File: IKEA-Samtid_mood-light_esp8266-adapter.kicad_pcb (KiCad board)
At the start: 2 copper layers, 17.5 x 20.5 mm, 5 parts, among them P1 ESP8266, P2 mood-light, U1 AMS1117-3.3

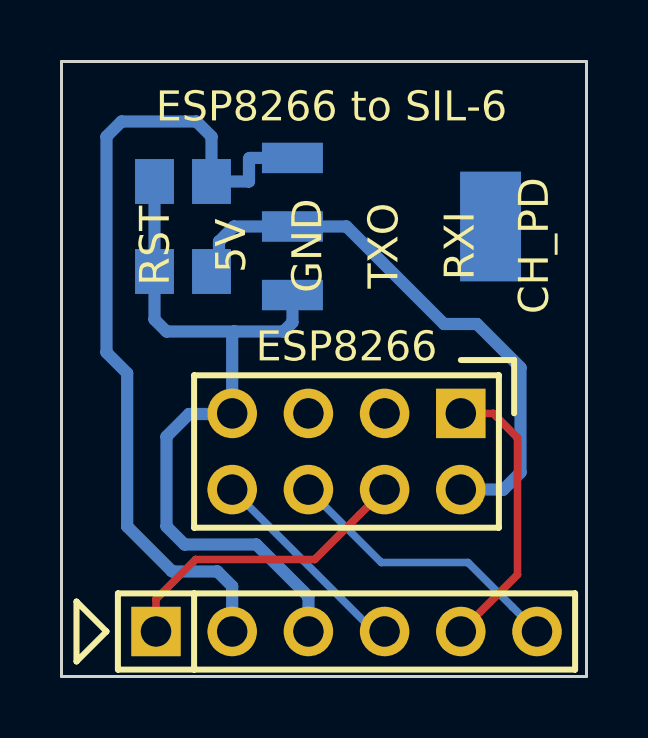
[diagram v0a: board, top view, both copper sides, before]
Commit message: ESP8266 adapter board reduced in size.
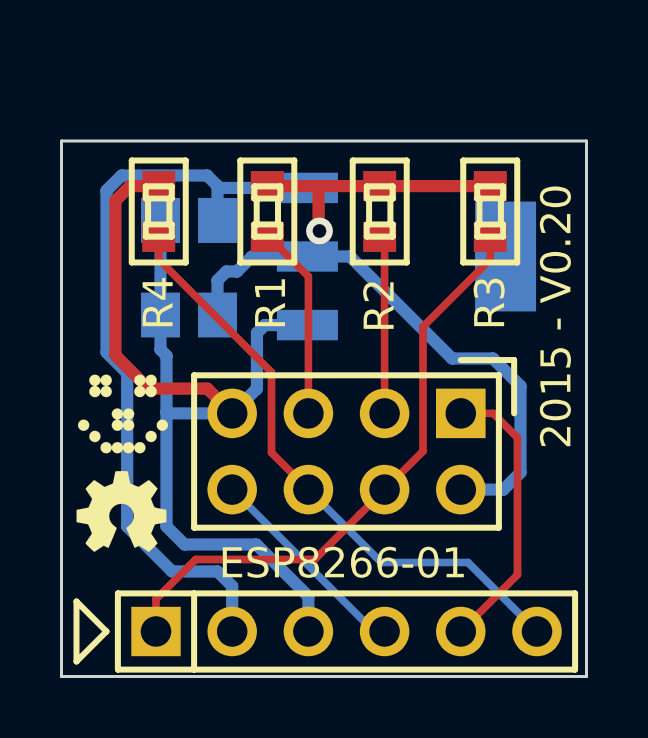
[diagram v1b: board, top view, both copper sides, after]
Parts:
- added G***: LED_smile_silkscreen_3mm, led-smile:LED_smile_silkscreen_3mm, F.Cu at (157.1, 109.8)
- added G***: OSHW-logo_silkscreen_3mm, oshw-logo:OSHW-logo_silkscreen_3mm, F.Cu at (157.0, 113.0)
- added R1: 10k, my_parts:MADW__R0603_2, F.Cu at (161.9, 103.0)
- added R2: 10k, my_parts:MADW__R0603_2, F.Cu at (165.6, 103.0)
- added R3: 10k, my_parts:MADW__R0603_2, F.Cu at (169.3, 103.0)
- added R4: 10k, my_parts:MADW__R0603_2, F.Cu at (158.2, 103.0)
- P1: value ESP8266 -> ESP8266-01
- moved C2 1.46 mm to (159.3, 106.5)
- moved C1 1.32 mm to (159.2, 103.3)
- moved U1 1.12 mm to (166.5, 104.5)
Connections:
- P1 pad 1: /RXI -> /TXO
- P1 pad 3: (no net) -> Net-(P1-Pad3)
- P1 pad 5: (no net) -> Net-(P1-Pad5)
- P1 pad 8: /TXO -> /RXI
- P2 pad 4: /TXO -> /RXI
- P2 pad 5: /RXI -> /TXO
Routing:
- net /CH_PD: track 9.58 -> 20.1 mm
- net GND: track 25.5 -> 35.7 mm
- net /RST: track 10.2 -> 20.1 mm
- net +3.3V: track 19.0 -> 28.4 mm, vias 0 -> 1
- net Net-(P1-Pad5): track 0.00 -> 6.48 mm
- net Net-(P1-Pad3): track 0.00 -> 5.95 mm
- net +5V: track 28.4 -> 25.5 mm
- net /TXO: track 7.39 -> 9.47 mm
- net /RXI: track 9.47 -> 7.39 mm
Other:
- board size 17.5 x 20.5 mm -> 17.5 x 17.8 mm
- net class Power: via_drill 0.635 -> 0.4572
- board text added: "-"
- board text added: "/CH_PD"
- board text added: "/RST"
- board text added: "2015 - V0.20"
- board text added: "3.3V SIG. !"
- board text added: "RX"
- board text added: "TX"
- board text removed: "CH_PD"
- board text removed: "ESP8266 to SIL-6"
- board text removed: "GND"
- board text removed: "RST"
- board text removed: "RXI"
- board text removed: "TXO"

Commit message: ESP8266 adapter tweaks.
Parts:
- U1: value AMS1117-3.3 -> AMS1117
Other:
- board text added: "2015 - V0.20.b"
- board text added: "AMS1117"
- board text removed: "2015 - V0.20"

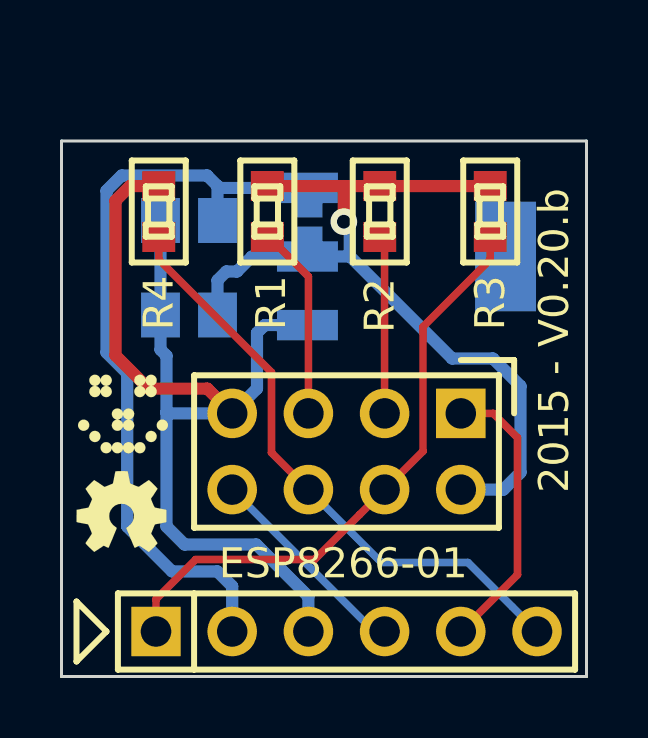
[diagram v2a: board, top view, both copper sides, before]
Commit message: Added pads for ESP8266 FW upd. mode (GPIO0 shorted to GND) on startup.
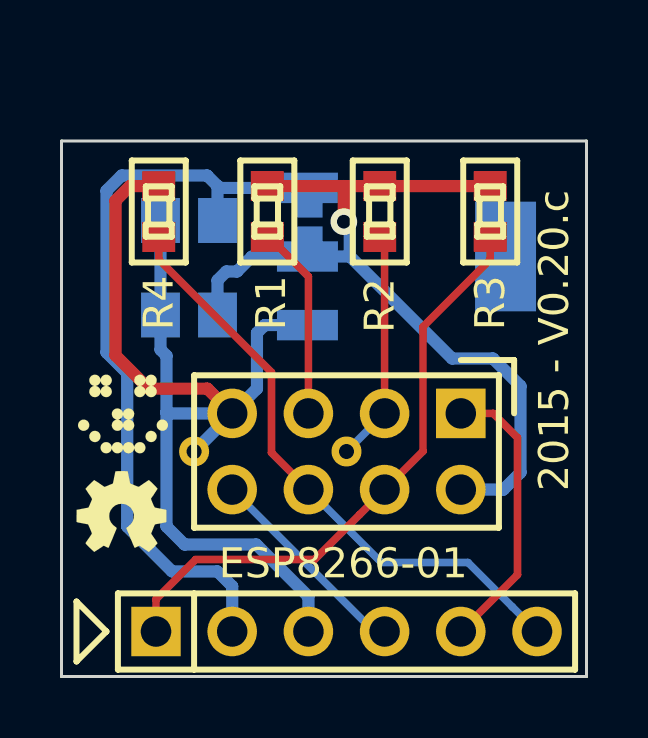
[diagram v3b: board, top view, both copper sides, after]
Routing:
- net Net-(P1-Pad3): track 5.95 -> 7.74 mm
- net GND: track 35.7 -> 37.5 mm
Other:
- board text added: "2015 - V0.20.c"
- board text added: "3.3V SIG"
- board text added: "FW UP"
- board text removed: "2015 - V0.20.b"
- board text removed: "3.3V SIG. !"
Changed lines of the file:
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@@
 (kicad_pcb (version 4) (host pcbnew "(2015-03-12 BZR 5508)-product")
   (general
-    (links 27)
-    (no_connects 3)
+    (links 24)
+    (no_connects 0)
     (area 154.481657 100.599999 181.95 123.450001)
     (thickness 1.6)
-    (drawings 15)
-    (tracks 95)
+    (drawings 16)
+    (tracks 97)
     (zones 0)
     (modules 11)
@@
     (title IKEA-Samtid_mood-light_esp8266-adapter)
     (date "Thu 12 Mar 2015")
-    (rev 0.20.b)
+    (rev 0.20.c)
     (company "2015 - blog.spitzenpfeil.org")
   )
@@
     (add_net GND)
   )
+  (module DIL-Headers:DIL-4 (layer F.Cu)
+    (at 164.5 111)
+    (descr "Male 3x2 header with 2.54mm raster")
+    (tags "CONN, header, male, 3x2, 2.54mm")
+    (fp_text reference P1 (at 0 -3.81) (layer F.SilkS) hide
+      (effects (font (size 1 1) (thickness 0.2)))
+    )
+    (fp_text value ESP8266-01 (at -0.11 3.73) (layer F.SilkS)
+      (effects (font (size 1 1) (thickness 0.2)))
+    )
+    (fp_line (start -4.191 0) (end -0.889 0) (layer B.SilkS) (width 0.2))
+    (fp_circle (center -5.08 0) (end -4.318 0) (layer B.SilkS) (width 0.2))
+    (fp_circle (center 0 0) (end 0.762 0) (layer B.SilkS) (width 0.2))
+    (fp_line (start 5.588 -3.048) (end 5.588 -1.27) (layer F.SilkS) (width 0.2))
+    (fp_line (start 3.81 -3.048) (end 5.588 -3.048) (layer F.SilkS) (width 0.2))
+    (fp_line (start 5.08 -2.54) (end 5.08 2.54) (layer F.SilkS) (width 0.2))
+    (fp_line (start -5.08 -2.54) (end 5.08 -2.54) (layer F.SilkS) (width 0.2))
+    (fp_line (start 5.08 2.54) (end -5.08 2.54) (layer F.SilkS) (width 0.2))
+    (fp_line (start -5.08 2.54) (end -5.08 -2.54) (layer F.SilkS) (width 0.2))
+    (pad 1 thru_hole rect (at 3.81 -1.27) (size 1.651 1.651) (drill 1.016) (layers *.Cu *.Mask F.SilkS)
+      (net 7 /TXO))
+    (pad 2 thru_hole circle (at 3.81 1.27) (size 1.651 1.651) (drill 1.016) (layers *.Cu *.Mask F.SilkS)
+      (net 3 +3.3V))
+    (pad 3 thru_hole circle (at 1.27 -1.27) (size 1.651 1.651) (drill 1.016) (layers *.Cu *.Mask F.SilkS)
+      (net 8 "Net-(P1-Pad3)"))
+    (pad 4 thru_hole circle (at 1.27 1.27) (size 1.651 1.651) (drill 1.016) (layers *.Cu *.Mask F.SilkS)
+      (net 5 /RST))
+    (pad 5 thru_hole circle (at -1.27 -1.27) (size 1.651 1.651) (drill 1.016) (layers *.Cu *.Mask F.SilkS)
+      (net 9 "Net-(P1-Pad5)"))
+    (pad 6 thru_hole circle (at -1.27 1.27) (size 1.651 1.651) (drill 1.016) (layers *.Cu *.Mask F.SilkS)
+      (net 6 /CH_PD))
+    (pad 7 thru_hole circle (at -3.81 -1.27) (size 1.651 1.651) (drill 1.016) (layers *.Cu *.Mask F.SilkS)
+      (net 2 GND))
+    (pad 8 thru_hole circle (at -3.81 1.27) (size 1.651 1.651) (drill 1.016) (layers *.Cu *.Mask F.SilkS)
+      (net 4 /RXI))
+    (pad 3 thru_hole circle (at 0 0) (size 1 1) (drill 0.5) (layers *.Cu *.Mask F.SilkS)
+      (net 8 "Net-(P1-Pad3)"))
+    (pad 7 thru_hole circle (at -5.08 0) (size 1 1) (drill 0.5) (layers *.Cu *.Mask F.SilkS)
+      (net 2 GND))
+  )
   (module SMD_Packages:SOT-223 (layer B.Cu)
     (at 166.5 104.5 90)
@@
     (pad 6 thru_hole circle (at 6.35 0) (size 1.65 1.65) (drill 1.016) (layers *.Cu *.Mask F.SilkS)
       (net 6 /CH_PD))
-  )
-  (module DIL-Headers:DIL-4 (layer F.Cu)
-    (at 164.5 111)
-    (descr "Male 3x2 header with 2.54mm raster")
-    (tags "CONN, header, male, 3x2, 2.54mm")
-    (fp_text reference P1 (at 0 -3.81) (layer F.SilkS) hide
-      (effects (font (size 1 1) (thickness 0.2)))
-    )
-    (fp_text value ESP8266-01 (at -0.11 3.73) (layer F.SilkS)
-      (effects (font (size 1 1) (thickness 0.2)))
-    )
-    (fp_line (start 5.588 -3.048) (end 5.588 -1.27) (layer F.SilkS) (width 0.2))
-    (fp_line (start 3.81 -3.048) (end 5.588 -3.048) (layer F.SilkS) (width 0.2))
-    (fp_line (start 5.08 -2.54) (end 5.08 2.54) (layer F.SilkS) (width 0.2))
-    (fp_line (start -5.08 -2.54) (end 5.08 -2.54) (layer F.SilkS) (width 0.2))
-    (fp_line (start 5.08 2.54) (end -5.08 2.54) (layer F.SilkS) (width 0.2))
-    (fp_line (start -5.08 2.54) (end -5.08 -2.54) (layer F.SilkS) (width 0.2))
-    (pad 1 thru_hole rect (at 3.81 -1.27) (size 1.651 1.651) (drill 1.016) (layers *.Cu *.Mask F.SilkS)
-      (net 7 /TXO))
-    (pad 2 thru_hole circle (at 3.81 1.27) (size 1.651 1.651) (drill 1.016) (layers *.Cu *.Mask F.SilkS)
-      (net 3 +3.3V))
-    (pad 3 thru_hole circle (at 1.27 -1.27) (size 1.651 1.651) (drill 1.016) (layers *.Cu *.Mask F.SilkS)
-      (net 8 "Net-(P1-Pad3)"))
-    (pad 4 thru_hole circle (at 1.27 1.27) (size 1.651 1.651) (drill 1.016) (layers *.Cu *.Mask F.SilkS)
-      (net 5 /RST))
-    (pad 5 thru_hole circle (at -1.27 -1.27) (size 1.651 1.651) (drill 1.016) (layers *.Cu *.Mask F.SilkS)
-      (net 9 "Net-(P1-Pad5)"))
-    (pad 6 thru_hole circle (at -1.27 1.27) (size 1.651 1.651) (drill 1.016) (layers *.Cu *.Mask F.SilkS)
-      (net 6 /CH_PD))
-    (pad 7 thru_hole circle (at -3.81 -1.27) (size 1.651 1.651) (drill 1.016) (layers *.Cu *.Mask F.SilkS)
-      (net 2 GND))
-    (pad 8 thru_hole circle (at -3.81 1.27) (size 1.651 1.651) (drill 1.016) (layers *.Cu *.Mask F.SilkS)
-      (net 4 /RXI))
   )
   (module my_parts:MADW__R0603_2 (layer F.Cu)
@@
       (xy -0.90932 1.3462)) (layer F.SilkS) (width 0.00254))
   )
+  (gr_text "FW\nUP" (at 158.04 109.29 90) (layer B.SilkS)
+    (effects (font (size 1 1) (thickness 0.2)) (justify mirror))
+  )
   (gr_text AMS1117 (at 166.4 104.55 90) (layer B.SilkS)
-    (effects (font (size 1 1) (thickness 0.25)) (justify mirror))
-  )
-  (gr_text "2015 - V0.20.b" (at 171.42 107.3 90) (layer F.SilkS)
-    (effects (font (size 1 1) (thickness 0.25)))
+    (effects (font (size 1 1) (thickness 0.2)) (justify mirror))
+  )
+  (gr_text "2015 - V0.20.c" (at 171.42 107.3 90) (layer F.SilkS)
+    (effects (font (size 1 1) (thickness 0.2)))
   )
   (dimension 17.85 (width 0.3) (layer Eco1.User)
@@
     (arrow2b (pts (xy 173.95 118.5) (xy 173.363579 117.373496)))
   )
-  (gr_text "3.3V SIG. !" (at 155.97 114.13 90) (layer B.SilkS)
-    (effects (font (size 1 1) (thickness 0.25)) (justify mirror))
-  )
-  (gr_text /CH_PD (at 170.815 112.776 90) (layer B.SilkS)
-    (effects (font (size 1 1) (thickness 0.25)) (justify mirror))
-  )
-  (gr_text RX (at 168.275 114.554 90) (layer B.SilkS)
-    (effects (font (size 1 1) (thickness 0.25)) (justify mirror))
-  )
-  (gr_text TX (at 165.862 114.554 90) (layer B.SilkS)
-    (effects (font (size 1 1) (thickness 0.25)) (justify mirror))
-  )
-  (gr_text - (at 163.195 114.554 90) (layer B.SilkS)
-    (effects (font (size 1 1) (thickness 0.25)) (justify mirror))
-  )
-  (gr_text 5V (at 160.655 114.427 90) (layer B.SilkS)
-    (effects (font (size 1 1) (thickness 0.25)) (justify mirror))
-  )
-  (gr_text /RST (at 158.17 113.38 90) (layer B.SilkS)
-    (effects (font (size 1 1) (thickness 0.25)) (justify mirror))
+  (gr_text "3.3V SIG" (at 155.94 115.02 90) (layer B.SilkS)
+    (effects (font (size 1 1) (thickness 0.2)) (justify mirror))
+  )
+  (gr_text /CH_PD (at 170.85 112.97 90) (layer B.SilkS)
+    (effects (font (size 1 1) (thickness 0.2)) (justify mirror))
+  )
+  (gr_text RX (at 168.3 114.87 90) (layer B.SilkS)
+    (effects (font (size 1 1) (thickness 0.2)) (justify mirror))
+  )
+  (gr_text TX (at 165.78 114.99 90) (layer B.SilkS)
+    (effects (font (size 1 1) (thickness 0.2)) (justify mirror))
+  )
+  (gr_text - (at 163.15 115.31 90) (layer B.SilkS)
+    (effects (font (size 1 1) (thickness 0.2)) (justify mirror))
+  )
+  (gr_text 5V (at 160.66 114.89 90) (layer B.SilkS)
+    (effects (font (size 1 1) (thickness 0.2)) (justify mirror))
+  )
+  (gr_text /RST (at 158.17 113.92 90) (layer B.SilkS)
+    (effects (font (size 1 1) (thickness 0.2)) (justify mirror))
   )
   (dimension 17.5 (width 0.3) (layer Eco1.User)
@@
   (segment (start 158.30004 106.44996) (end 158.30008 106.45) (width 0.4064) (layer B.Cu) (net 2))
   (segment (start 158.30004 103.3) (end 158.30004 106.44996) (width 0.4064) (layer B.Cu) (net 2))
+  (segment (start 159.42 111) (end 160.69 109.73) (width 0.4064) (layer B.Cu) (net 2))
   (segment (start 164.6204 104.5) (end 164.61 104.4896) (width 0.4064) (layer B.Cu) (net 3))
   (segment (start 164.61 104.4896) (end 164.61 103.538739) (width 0.4064) (layer B.Cu) (net 3))
@@
   (segment (start 165.77 104.01036) (end 165.608 103.84836) (width 0.254) (layer F.Cu) (net 8))
   (segment (start 165.77 109.73) (end 165.77 104.01036) (width 0.254) (layer F.Cu) (net 8))
+  (segment (start 164.5 111) (end 165.77 109.73) (width 0.254) (layer B.Cu) (net 8))
   (segment (start 161.9123 103.84836) (end 161.8615 103.84836) (width 0.254) (layer F.Cu) (net 9))
   (segment (start 163.23 105.16606) (end 161.9123 103.84836) (width 0.254) (layer F.Cu) (net 9))

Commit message: ESP8266 adapter: changed RX/TX netnames to avoid confusion.
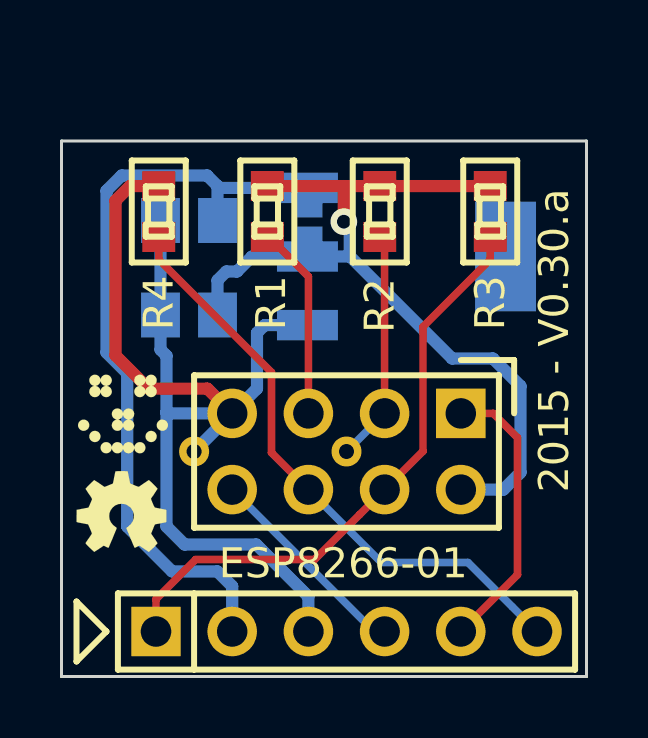
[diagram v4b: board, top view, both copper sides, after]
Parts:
- U1: value AMS1117 -> AMS1117-3.3
- renumbered G*** to G1, G*** to G2
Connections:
- P1 pad 1: /TXO -> /RXI
- P1 pad 8: /RXI -> /TXO
- P2 pad 4: /RXI -> /TXO
- P2 pad 5: /TXO -> /RXI
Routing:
- net /TXO: track 9.47 -> 7.39 mm
- net /RXI: track 7.39 -> 9.47 mm
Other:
- board text added: "2015 - V0.30.a"
- board text removed: "2015 - V0.20.c"

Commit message: ESP8266 adapter: silkscreen tweaks (show pull-up/down status).
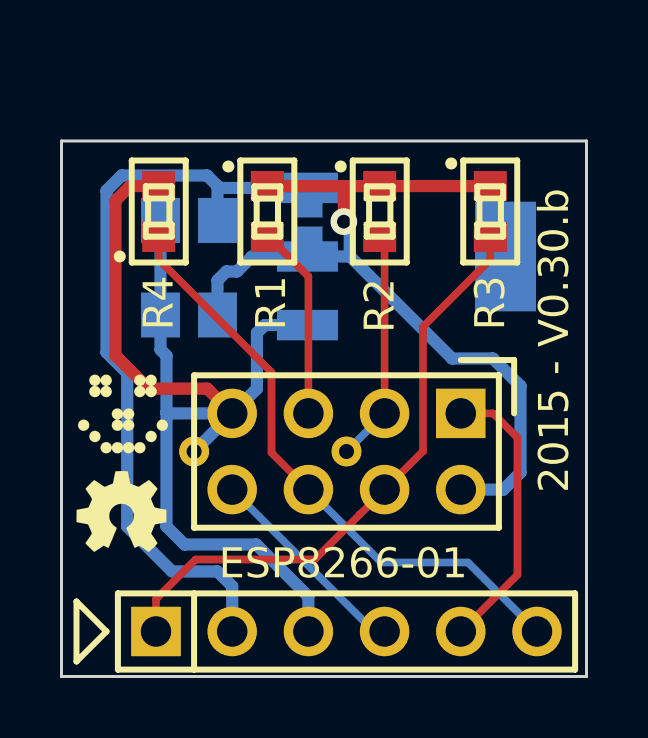
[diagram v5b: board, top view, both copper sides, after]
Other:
- board text added: "2015 - V0.30.b"
- board text added: "~CH_PD~↓"
- board text added: "~RST~↑"
- board text removed: "/CH_PD"
- board text removed: "/RST"
- board text removed: "2015 - V0.30.a"

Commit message: ESP8266 adapter tweaks + added shortened github link on copper.
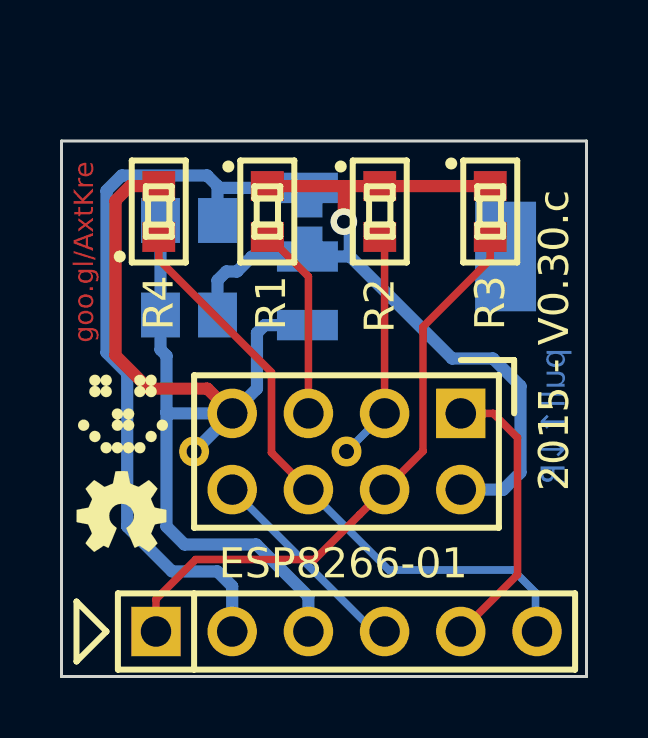
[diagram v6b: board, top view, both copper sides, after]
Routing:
- net /CH_PD: track 20.1 -> 20.8 mm
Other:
- board text added: "2015 - V0.30.c"
- board text added: "AUX 3.3V reg."
- board text added: "EN↓"
- board text added: "goo.gl/AxtKre"
- board text added: "pull↑↓R"
- board text removed: "2015 - V0.30.b"
- board text removed: "~CH_PD~↓"
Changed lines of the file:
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@@
     (area 154.481657 100.599999 181.95 123.450001)
     (thickness 1.6)
-    (drawings 16)
-    (tracks 97)
+    (drawings 19)
+    (tracks 98)
     (zones 0)
     (modules 11)
@@
     (title IKEA-Samtid_mood-light_esp8266-adapter)
     (date "Fri 13 Mar 2015")
-    (rev 0.30.b)
+    (rev 0.30.c)
     (company "2015 - blog.spitzenpfeil.org")
   )
@@
     (mod_text_width 0.15)
     (pad_size 1 1)
-    (pad_drill 0)
+    (pad_drill 0.5)
     (pad_to_mask_clearance 0.0254)
     (aux_axis_origin 0 0)
@@
     (pad 8 thru_hole circle (at -3.81 1.27) (size 1.651 1.651) (drill 1.016) (layers *.Cu *.Mask F.SilkS)
       (net 7 /TXO))
-    (pad 3 thru_hole circle (at 0 0) (size 1 1) (drill 0.5) (layers *.Cu *.Mask F.SilkS)
+    (pad 3 thru_hole circle (at 0 0) (size 1 1) (drill 0.5) (layers *.Cu B.Mask)
       (net 8 "Net-(P1-Pad3)"))
-    (pad 7 thru_hole circle (at -5.08 0) (size 1 1) (drill 0.5) (layers *.Cu *.Mask F.SilkS)
+    (pad 7 thru_hole circle (at -5.08 0) (size 1 1) (drill 0.5) (layers *.Cu B.Mask)
       (net 2 GND))
   )
@@
       (xy -0.90932 1.3462)) (layer F.SilkS) (width 0.00254))
   )
+  (gr_text pull↑↓R (at 171.4 109.85 90) (layer B.Cu)
+    (effects (font (size 0.8 0.8) (thickness 0.16)) (justify mirror))
+  )
+  (gr_text goo.gl/AxtKre (at 155.75 104.35 90) (layer F.Cu)
+    (effects (font (size 0.65 0.65) (thickness 0.16)))
+  )
+  (gr_text "AUX\n3.3V reg." (at 165.6 104.65 90) (layer B.SilkS)
+    (effects (font (size 0.85 1) (thickness 0.2)) (justify mirror))
+  )
   (gr_text "FW\nUP" (at 158.04 109.29 90) (layer B.SilkS)
     (effects (font (size 1 1) (thickness 0.2)) (justify mirror))
   )
-  (gr_text AMS1117 (at 166.4 104.55 90) (layer B.SilkS)
+  (gr_text AMS1117 (at 167.95 104.55 90) (layer B.SilkS)
     (effects (font (size 1 1) (thickness 0.2)) (justify mirror))
   )
-  (gr_text "2015 - V0.30.b" (at 171.42 107.3 90) (layer F.SilkS)
+  (gr_text "2015 - V0.30.c" (at 171.42 107.3 90) (layer F.SilkS)
     (effects (font (size 1 1) (thickness 0.2)))
   )
@@
     (effects (font (size 1 1) (thickness 0.2)) (justify mirror))
   )
-  (gr_text ~CH_PD~↓ (at 170.94 113.13 90) (layer B.SilkS)
+  (gr_text EN↓ (at 170.85 114.55 90) (layer B.SilkS)
     (effects (font (size 1 1) (thickness 0.2)) (justify mirror))
   )
@@
   (segment (start 163.44 114.6) (end 164.944501 113.095499) (width 0.254) (layer F.Cu) (net 5))
   (segment (start 164.944501 113.095499) (end 165.77 112.27) (width 0.254) (layer F.Cu) (net 5))
+  (segment (start 163.23 112.27) (end 165.91 114.95) (width 0.254) (layer B.Cu) (net 6))
+  (segment (start 165.91 114.95) (end 170.05 114.95) (width 0.254) (layer B.Cu) (net 6))
+  (segment (start 170.05 114.95) (end 170.8 115.7) (width 0.254) (layer B.Cu) (net 6))
+  (segment (start 170.8 115.7) (end 170.8 116.95) (width 0.254) (layer B.Cu) (net 6))
+  (segment (start 170.8 116.95) (end 170.85 117) (width 0.254) (layer B.Cu) (net 6))
   (segment (start 163.23 112.27) (end 162 111.04) (width 0.254) (layer F.Cu) (net 6))
   (segment (start 162 111.04) (end 162 108.35947) (width 0.254) (layer F.Cu) (net 6))
   (segment (start 162 108.35947) (end 158.242 104.60147) (width 0.254) (layer F.Cu) (net 6))
   (segment (start 158.242 104.60147) (end 158.242 103.84836) (width 0.254) (layer F.Cu) (net 6))
-  (segment (start 163.23 112.27) (end 165.66 114.7) (width 0.254) (layer B.Cu) (net 6))
-  (segment (start 170.025001 116.175001) (end 170.85 117) (width 0.254) (layer B.Cu) (net 6))
-  (segment (start 165.66 114.7) (end 168.55 114.7) (width 0.254) (layer B.Cu) (net 6))
-  (segment (start 168.55 114.7) (end 170.025001 116.175001) (width 0.254) (layer B.Cu) (net 6))
   (segment (start 165.42 117) (end 165.77 117) (width 0.254) (layer B.Cu) (net 7))
   (segment (start 165.42 117) (end 165.77 117) (width 0.254) (layer F.Cu) (net 7))
